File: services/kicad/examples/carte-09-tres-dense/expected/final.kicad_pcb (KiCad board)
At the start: 2 copper layers, 130 x 100 mm, 62 parts, among them J1 IN_5V, J2 SWD, J3 IO0, J4 IO1, J5 IO2, J6 IO3, J7 IO4, U1 STM32F103C8T6, U2 AMS1117-3.3

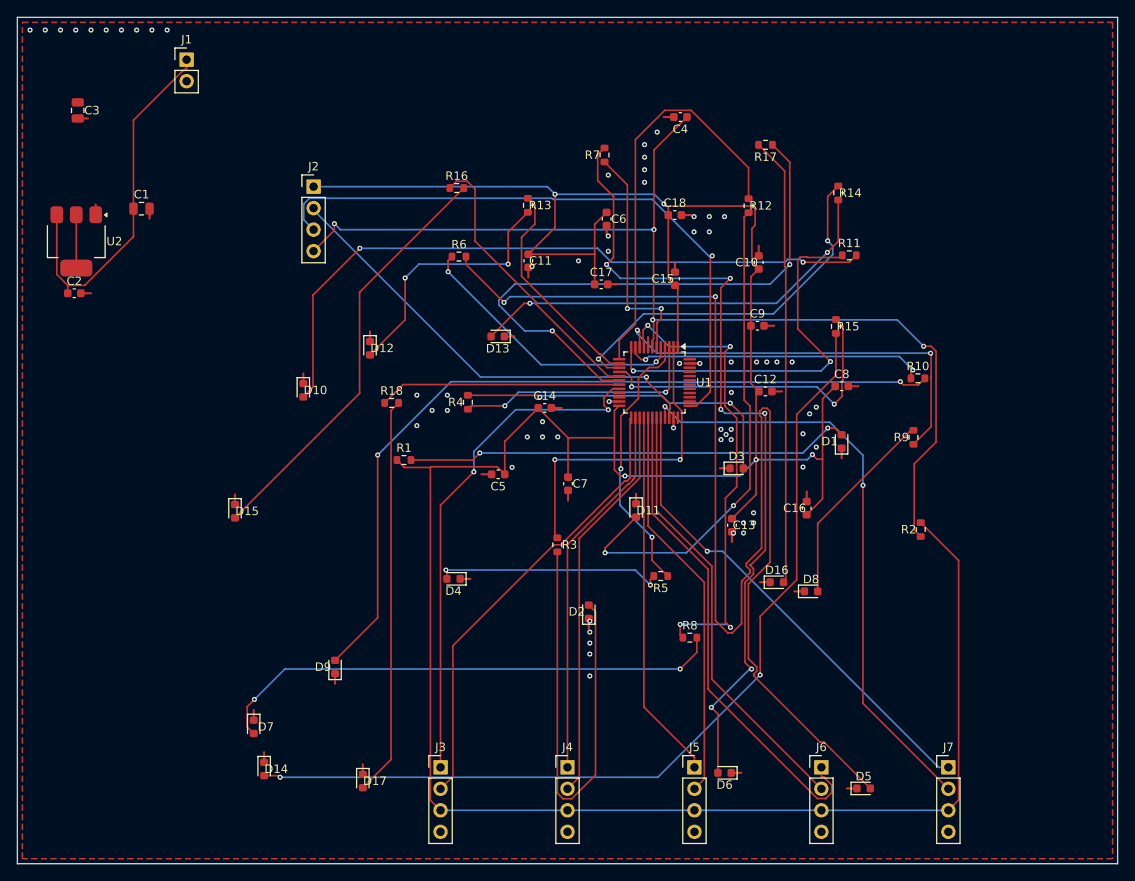
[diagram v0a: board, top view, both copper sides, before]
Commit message: test(examples): les dix cartes du banc sont routees a 100 % et fabricables
De 5 a 70 composants, toutes verifiees sur le BOARD LIVRE par kicad-cli :
100 % routees, zero connexion manquante, zero violation de severite error.

La carte 09 a debloque en lui ouvrant un plafond a quatre couches — et elle ne
s en est PAS servie : elle a reussi au premier palier, sur deux couches. C est
le comportement attendu, le plafond ne prescrit rien. Les dix boards livres ne
portent que F.Cu et B.Cu, y compris celui de 70 composants, et deux couches
coutent moins cher a fabriquer que quatre. Le banc des huit cartes historiques
avait fait le meme constat le 2026-09-03.

⚠️ Avant aujourd hui AUCUN schema ne declarait `max_layers`, alors que la
description de la carte 09 annoncait « plafond 4 couches » : la documentation
promettait une capacite que le fichier ne declarait pas. Meme faute qu une
section d ordre d execution laissee perimee dans CLAUDE.md, qui avait fait
conclure a une cascade mal ordonnee.

⚠️ Deux tirages ne prouvent rien, et les deux cartes recalcitrantes le montrent.
La carte 07 a rendu 5, puis 2, puis 3 erreurs, puis 0 % route, avant d atteindre
zero. La carte 09 a rendu 1 erreur, puis 2 au tirage suivant, puis zero. Le
placement et le routage sont stochastiques tous les deux — ce depot mesure deja
23 points d ecart entre deux tirages d une meme carte au meme placement. C est
exactement sur deux tirages concordants que j avais conclu, a tort, a un defaut
structurel.

Co-Authored-By: Claude Opus 5 <noreply@anthropic.com>
Claude-Session: https://claude.ai/code/session_01TnMqm4La2CxQHHB5K8aSSV
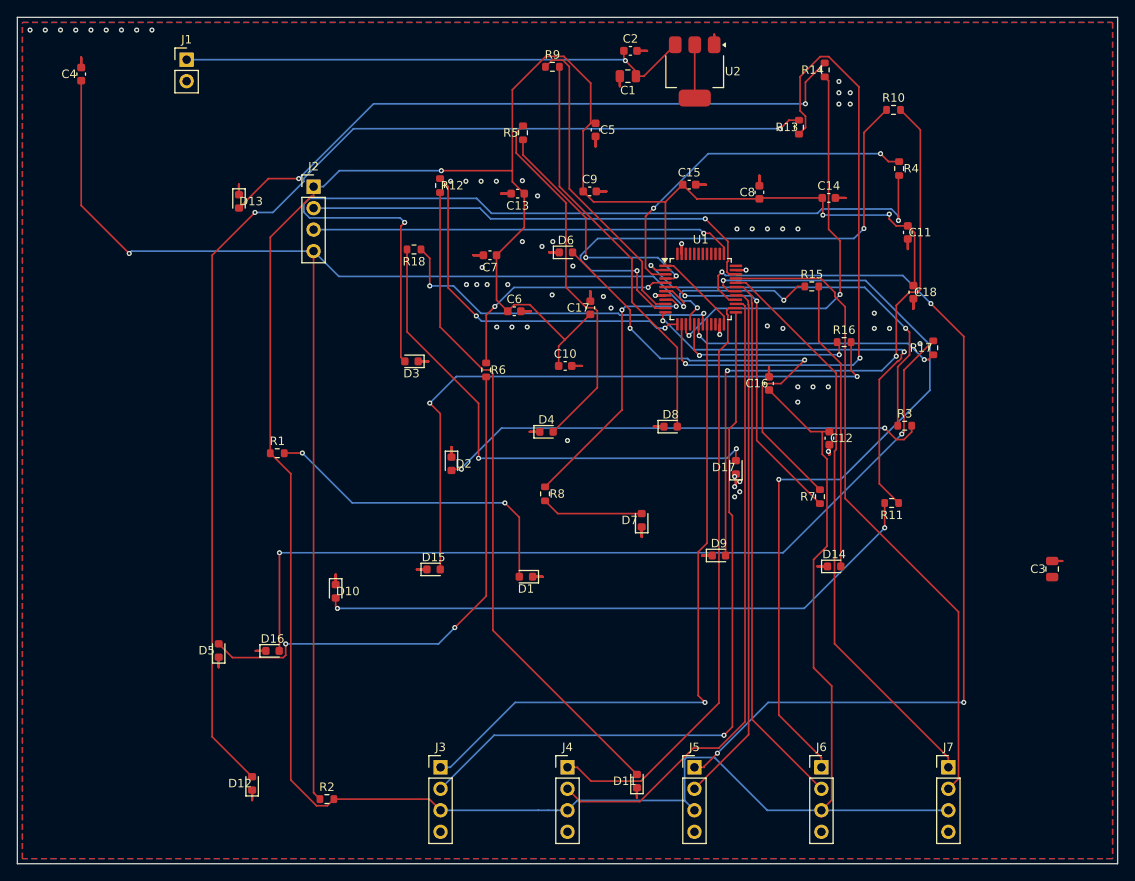
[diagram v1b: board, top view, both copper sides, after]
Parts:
- moved C3 127.2 mm to (205.8, 120.2), turned to 90 degrees
- moved D5 77.9 mm to (107.3, 129.8), turned to 90 degrees
- moved R2 77.1 mm to (120.1, 147.4), turned to 0 degrees
- moved U2 75.8 mm to (163.5, 61.4)
- moved C2 71.7 mm to (155.9, 59.0)
- moved D14 71.5 mm to (180.0, 119.9), turned to 0 degrees
- moved C4 71.0 mm to (91.0, 61.7), turned to 90 degrees
- moved D6 64.3 mm to (148.3, 82.8), turned to 0 degrees
- moved R9 61.1 mm to (146.7, 60.8), turned to 0 degrees
- moved D16 60.1 mm to (113.6, 129.9)
- moved C1 59.6 mm to (155.6, 62.0), turned to 180 degrees
- moved R4 57.9 mm to (187.7, 72.9), turned to -90 degrees
- moved D17 57.6 mm to (168.4, 108.2), turned to 90 degrees
- moved R5 54.8 mm to (143.2, 68.6), turned to 90 degrees
- moved D12 53.3 mm to (111.2, 145.5), turned to 90 degrees
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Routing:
- net LEDA10: track 30.8 -> 139.7 mm
- net GND: track 48.0 -> 144.0 mm, vias 65 -> 61
- net LEDA3: track 155.1 -> 62.0 mm
- net LEDA12: track 107.8 -> 34.2 mm, vias 2 -> 0
- net EXT2_1: track 43.8 -> 114.9 mm, vias 0 -> 4
- net LEDA1: track 39.9 -> 107.9 mm
- net LEDA14: track 53.1 -> 103.5 mm, vias 0 -> 2
- net LEDA5: track 61.0 -> 12.0 mm, vias 2 -> 0
- net IO_L10: track 26.0 -> 74.8 mm, vias 0 -> 2
- net LEDA4: track 98.5 -> 55.4 mm, vias 6 -> 2
- net IO_L14: track 69.6 -> 30.4 mm
- net EXT3_1: track 58.7 -> 93.6 mm, vias 0 -> 2
- net EXT0_2: track 53.8 -> 87.0 mm, vias 0 -> 1
- net NRST: track 129.6 -> 159.4 mm, vias 4 -> 2
- net IO_L7: track 35.7 -> 64.2 mm
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
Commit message: feat(examples): carte-09 livree (100 %, 0 erreur, 2 couches) ; scripts/vues_index.py genere VUES.md
carte-09 : grille 3 -> 82 %, paires 55 -> 34 mm ; decouplage 14 -> 19 mm (le
snap ne trouve pas de place contre les broches d un LQFP entoure de 62
composants -- a traiter). Placement livre a cote du board route.

Co-Authored-By: Claude Fable 5.1 <noreply@anthropic.com>
Claude-Session: https://claude.ai/code/session_01TnMqm4La2CxQHHB5K8aSSV
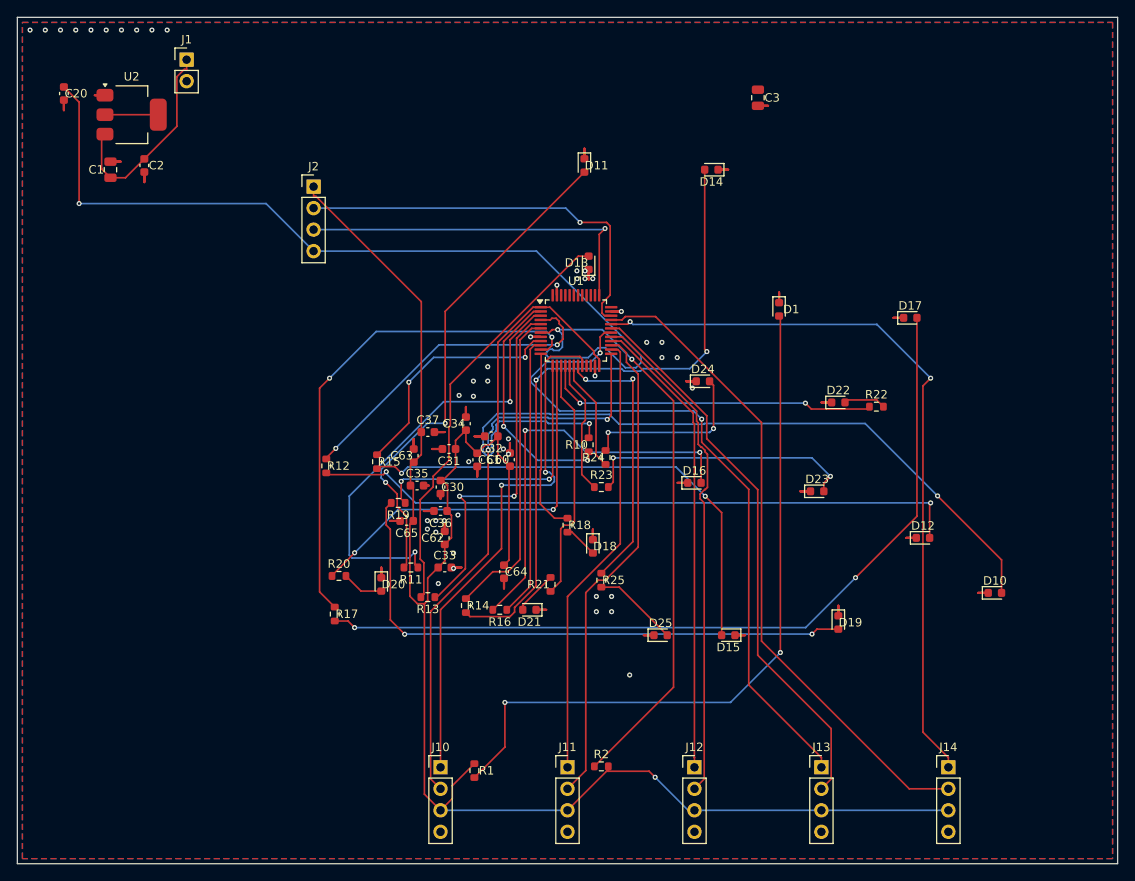
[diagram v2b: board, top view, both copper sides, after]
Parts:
- removed C10, C11, C12, C13, C14, C15, C16, C17, C18, C4, C5, C6, C7, C8, C9: 100nF, C_0603_1608Metric
- removed D2, D3, D4, D5, D6, D7, D8, D9: LED, LED_0603_1608Metric
- removed J3: IO0, PinHeader_1x04_P2.54mm_Vertical
- removed J4: IO1, PinHeader_1x04_P2.54mm_Vertical
- removed J5: IO2, PinHeader_1x04_P2.54mm_Vertical
- removed J6: IO3, PinHeader_1x04_P2.54mm_Vertical
- removed J7: IO4, PinHeader_1x04_P2.54mm_Vertical
- removed R3, R4, R5, R6, R7, R8, R9: 1k, R_0603_1608Metric
- added C20: 100nF, C_0603_1608Metric, F.Cu at (89.0, 64.0)
- added C30: 100nF, C_0603_1608Metric, F.Cu at (133.5, 110.5)
- added C31: 100nF, C_0603_1608Metric, F.Cu at (134.5, 106.0)
- added C32: 100nF, C_0603_1608Metric, F.Cu at (139.5, 104.5)
- added C33: 100nF, C_0603_1608Metric, F.Cu at (134.0, 120.0)
- added C34: 100nF, C_0603_1608Metric, F.Cu at (136.5, 103.0)
- added C35: 100nF, C_0603_1608Metric, F.Cu at (130.7, 110.3)
- added C36: 100nF, C_0603_1608Metric, F.Cu at (133.5, 113.3)
- added C37: 100nF, C_0603_1608Metric, F.Cu at (132.0, 104.0)
- added C60: 100nF, C_0603_1608Metric, F.Cu at (141.7, 107.3)
- added C61: 100nF, C_0603_1608Metric, F.Cu at (137.8, 107.3)
- added C62: 100nF, C_0603_1608Metric, F.Cu at (134.0, 116.5)
- added C63: 100nF, C_0603_1608Metric, F.Cu at (130.3, 106.8)
- added C64: 100nF, C_0603_1608Metric, F.Cu at (141.0, 120.5)
- added C65: 100nF, C_0603_1608Metric, F.Cu at (129.5, 114.5)
- added D18: LED, LED_0603_1608Metric, F.Cu at (151.5, 117.5)
- added D19: LED, LED_0603_1608Metric, F.Cu at (180.5, 126.5)
- added D20: LED, LED_0603_1608Metric, F.Cu at (126.5, 122.0)
- added D21: LED, LED_0603_1608Metric, F.Cu at (144.0, 125.0)
- added D22: LED, LED_0603_1608Metric, F.Cu at (180.5, 100.5)
- added D23: LED, LED_0603_1608Metric, F.Cu at (178.0, 111.0)
- added D24: LED, LED_0603_1608Metric, F.Cu at (164.5, 98.0)
- added D25: LED, LED_0603_1608Metric, F.Cu at (159.5, 128.0)
- added J10: IO0, PinHeader_1x04_P2.54mm_Vertical, F.Cu at (133.5, 143.6)
- added J11: IO1, PinHeader_1x04_P2.54mm_Vertical, F.Cu at (148.5, 143.6)
- added J12: IO2, PinHeader_1x04_P2.54mm_Vertical, F.Cu at (163.5, 143.6)
- added J13: IO3, PinHeader_1x04_P2.54mm_Vertical, F.Cu at (178.5, 143.6)
- added J14: IO4, PinHeader_1x04_P2.54mm_Vertical, F.Cu at (193.5, 143.6)
- added R19: 1k, R_0603_1608Metric, F.Cu at (128.5, 112.4)
- added R20: 1k, R_0603_1608Metric, F.Cu at (121.5, 121.0)
- added R21: 1k, R_0603_1608Metric, F.Cu at (146.5, 122.0)
- added R22: 1k, R_0603_1608Metric, F.Cu at (185.0, 101.0)
- added R23: 1k, R_0603_1608Metric, F.Cu at (152.5, 110.5)
- added R24: 1k, R_0603_1608Metric, F.Cu at (153.0, 107.0)
- added R25: 1k, R_0603_1608Metric, F.Cu at (152.5, 121.5)
- moved D12 84.4 mm to (190.5, 116.5), turned to 0 degrees
- moved D10 77.9 mm to (199.0, 123.0), turned to 0 degrees
- moved R17 77.4 mm to (121.0, 125.5), turned to -90 degrees
- moved R14 76.2 mm to (136.5, 124.5), turned to -90 degrees
- moved D11 73.0 mm to (150.5, 72.5), turned to -90 degrees
- moved R13 70.7 mm to (132.0, 123.5), turned to 180 degrees
- moved U2 66.7 mm to (97.0, 66.5), turned to 0 degrees
- moved C3 65.6 mm to (171.0, 64.5), turned to -90 degrees
- moved C1 62.1 mm to (94.5, 73.0), turned to 90 degrees
- moved C2 59.0 mm to (98.5, 72.5), turned to -90 degrees
- moved R11 57.3 mm to (130.0, 120.0)
- moved R15 55.4 mm to (126.0, 107.5), turned to -90 degrees
- moved D16 53.7 mm to (163.5, 110.0)
- moved R10 53.5 mm to (151.0, 105.5), turned to 90 degrees
- moved R16 51.5 mm to (140.5, 125.0), turned to 180 degrees
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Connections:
- D10 pad 2: LEDA8 -> LEDA0
- D11 pad 2: LEDA9 -> LEDA1
- D12 pad 2: LEDA10 -> LEDA2
- D13 pad 2: LEDA11 -> LEDA3
- D14 pad 2: LEDA12 -> LEDA4
- D15 pad 2: LEDA13 -> LEDA5
- D16 pad 2: LEDA14 -> LEDA6
- D17 pad 2: LEDA15 -> LEDA7
- R10 pad 1: IO_L7 -> IO_L0
- R10 pad 2: LEDA7 -> LEDA0
- R11 pad 1: IO_L8 -> IO_L1
- R11 pad 2: LEDA8 -> LEDA1
- R12 pad 1: IO_L9 -> IO_L2
- R12 pad 2: LEDA9 -> LEDA2
- R13 pad 1: IO_L10 -> IO_L3
- R13 pad 2: LEDA10 -> LEDA3
- R14 pad 1: IO_L11 -> IO_L4
- R14 pad 2: LEDA11 -> LEDA4
- R15 pad 1: IO_L12 -> IO_L5
- R15 pad 2: LEDA12 -> LEDA5
- R16 pad 1: IO_L13 -> IO_L6
- R16 pad 2: LEDA13 -> LEDA6
- R17 pad 1: IO_L14 -> IO_L7
- R17 pad 2: LEDA14 -> LEDA7
- R18 pad 1: IO_L15 -> IO_L8
- R18 pad 2: LEDA15 -> LEDA8
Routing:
- net +3V3: track 383.1 -> 228.1 mm, vias 3 -> 1
- net LEDA10: track 139.7 -> 4.92 mm, vias 2 -> 0
- net LEDA14: track 103.5 -> 20.7 mm
- net LEDA11: track 77.8 -> 5.19 mm, vias 2 -> 0
- net LEDA8: track 72.9 -> 4.02 mm, vias 2 -> 0
- net EXT2_1: track 114.9 -> 55.1 mm, vias 4 -> 0
- net LEDA15: track 60.5 -> 10.1 mm, vias 2 -> 0
- net LEDA1: track 107.9 -> 59.3 mm
- net LED_PWR: track 37.9 -> 85.2 mm
- net LEDA5: track 12.0 -> 58.1 mm, vias 0 -> 2
- net LEDA13: track 76.3 -> 32.4 mm
- net VIN: track 61.7 -> 24.6 mm, vias 1 -> 0
- net LEDA0: track 58.2 -> 94.0 mm
- net LEDA2: track 43.2 -> 77.5 mm, vias 0 -> 2
- net IO_L8: track 51.3 -> 21.7 mm, vias 2 -> 0
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
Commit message: examples: carte-09 et carte-10 livrees a 100 % / 0 erreur (4 couches) -- placement a remplacer par la campagne en cours
Co-Authored-By: Claude Fable 5.1 <noreply@anthropic.com>

Claude-Session: https://claude.ai/code/session_01TnMqm4La2CxQHHB5K8aSSV
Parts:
- moved R13 91.3 mm to (207.0, 71.5), turned to 90 degrees
- moved R12 87.1 mm to (207.0, 103.0), turned to 90 degrees
- moved R17 87.1 mm to (207.0, 111.5), turned to 90 degrees
- moved R20 85.6 mm to (207.0, 116.0), turned to 90 degrees
- moved R19 84.7 mm to (207.0, 80.5), turned to 90 degrees
- moved R15 83.9 mm to (207.0, 129.5), turned to 90 degrees
- moved D20 83.2 mm to (209.5, 116.0), turned to 90 degrees
- moved R11 79.9 mm to (207.0, 98.5), turned to 90 degrees
- moved D14 78.9 mm to (209.5, 138.5), turned to 90 degrees
- moved C20 78.6 mm to (92.0, 142.5), turned to 0 degrees
- moved R14 71.9 mm to (207.0, 138.5), turned to 90 degrees
- moved D18 71.3 mm to (209.5, 76.0), turned to 90 degrees
- moved R18 70.3 mm to (207.0, 76.0), turned to 90 degrees
- moved D21 67.9 mm to (209.5, 107.0), turned to 90 degrees
- moved R16 67.1 mm to (207.0, 134.0), turned to 90 degrees
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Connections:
- C3 pad 1: Net-(C3-1) -> +3V3
- U1 pad 36: Net-(U1-36) -> +3V3
- U1 pad 48: Net-(U1-48) -> +3V3
- U2 pad 2: Net-(U2-2) -> +3V3
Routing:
- net GND: track 140.4 -> 243.6 mm, vias 47 -> 57
- net LEDA7: track 98.0 -> 2.52 mm, vias 2 -> 0
- net LEDA0: track 94.0 -> 2.52 mm, vias 2 -> 0
- net IO_L14: track 13.2 -> 97.0 mm, vias 0 -> 2
- net LEDA4: track 78.1 -> 2.52 mm, vias 2 -> 0
- net LEDA2: track 77.5 -> 2.52 mm, vias 2 -> 0
- net +3V3: track 228.1 -> 302.9 mm, vias 1 -> 2
- net VIN: track 24.6 -> 97.8 mm, vias 0 -> 1
- net IO_L5: track 28.3 -> 96.8 mm, vias 2 -> 3
- net IO_L4: track 37.3 -> 103.8 mm, vias 0 -> 2
- net IO_L6: track 33.4 -> 99.3 mm, vias 0 -> 2
- net LEDA9: track 68.2 -> 2.52 mm, vias 2 -> 0
- net LEDA1: track 59.3 -> 2.52 mm, vias 2 -> 0
- net LEDA5: track 58.1 -> 2.52 mm, vias 2 -> 0
- net IO_L0: track 28.5 -> 83.0 mm
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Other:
- copper layers 2 -> 4

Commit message: examples: carte-09 -- placement pro gele (3,2 mm de decouplage) route a 100 %, 0 erreur, 6 couches
Co-Authored-By: Claude Fable 5.1 <noreply@anthropic.com>

Claude-Session: https://claude.ai/code/session_01TnMqm4La2CxQHHB5K8aSSV
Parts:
- moved C3 68.2 mm to (90.0, 113.5)
- moved R16 58.0 mm to (205.5, 76.0)
- moved D16 58.0 mm to (209.5, 76.0)
- moved R22 44.5 mm to (205.5, 138.5)
- moved D22 44.5 mm to (209.5, 138.5)
- moved R1 41.8 mm to (150.0, 111.0), turned to -90 degrees
- moved R25 40.0 mm to (205.5, 129.5)
- moved D25 40.0 mm to (209.5, 129.5)
- moved C32 38.2 mm to (129.0, 94.5), turned to 0 degrees
- moved C64 36.8 mm to (142.5, 78.5), turned to -90 degrees
- moved U2 35.5 mm to (121.0, 61.5)
- moved C63 32.9 mm to (137.5, 81.5), turned to 0 degrees
- moved C60 32.9 mm to (128.0, 91.5), turned to 180 degrees
- moved C1 32.6 mm to (126.5, 64.5), turned to 90 degrees
- moved R13 31.5 mm to (205.5, 103.0)
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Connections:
- C3 pad 1: +3V3 -> Net-(C3-1)
- U1 pad 36: +3V3 -> Net-(U1-36)
- U1 pad 48: +3V3 -> Net-(U1-48)
- U2 pad 2: +3V3 -> Net-(U2-2)
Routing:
- net GND: track 243.6 -> 70.8 mm, vias 57 -> 78
- net +3V3: track 302.9 -> 234.3 mm, vias 2 -> 0
- net VIN: track 97.8 -> 34.3 mm, vias 1 -> 0
- net IO_L12: track 69.8 -> 118.5 mm
- net NRST: track 151.6 -> 112.7 mm, vias 3 -> 1
- net IO_L15: track 68.2 -> 101.7 mm
- net LED_PWR: track 49.3 -> 16.8 mm, vias 2 -> 0
- net IO_L14: track 97.0 -> 69.7 mm
- net IO_L6: track 99.3 -> 76.1 mm
- net IO_L9: track 60.7 -> 83.0 mm
- net IO_L4: track 103.8 -> 86.6 mm
- net IO_L7: track 81.4 -> 98.5 mm
- net IO_L10: track 89.6 -> 75.1 mm
- net IO_L13: track 64.9 -> 78.7 mm
- net IO_L3: track 65.3 -> 78.7 mm, vias 3 -> 2
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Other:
- copper layers 4 -> 6
